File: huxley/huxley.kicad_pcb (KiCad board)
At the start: 4 copper layers, 150 x 150 mm, 101 parts, among them J1 CT3151V1-2, J11 SMA_RF2-04A-T-00-50-G, J13 SMA_RF2-04A-T-00-50-G, J15 SMA_RF2-04A-T-00-50-G, J17 SMA_RF2-04A-T-00-50-G, J18 SMA_RF2-04A-T-00-50-G, J19 SMA_RF2-04A-T-00-50-G, J2 CT3151V1-2, J20 SMA_RF2-04A-T-00-50-G, J21 61300211121, J22 SMA_RF2-04A-T-00-50-G, J24 CT3151V1-2, J25 61300211121, J26 61300211121, J27 61300211121, J28 61300211121, J29 61300211121, J3 CT3151V1-2, J30 61300211121, J31 61300211121, J32 61300211121, J33 67996-130HLF, J34 CT3151V1-0, J35 CT3151V1-2, J37 CT3151V1-0, J39 CT3151V1-2, J4 SMA_RF2-04A-T-00-50-G, J5 SMA_RF2-04A-T-00-50-G, J7 SMA_RF2-04A-T-00-50-G, J9 SMA_RF2-04A-T-00-50-G, U2 LM134H, U3 MAX40201FAUA+, U4 TMUX1112PWR, U5 TMUX1112PWR, U6 NVT2010PW_118

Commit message: layout_1003_2
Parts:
- U1: footprint _726_Common:CPG08462 -> 0_726_footprints:CPG08462_Full
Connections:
- U1 pad A1: PP_VDDIO_1V8 -> unconnected-(U1D-VDDPST-PadA1)
- U1 pad A11: GND -> unconnected-(U1F-VSS-PadA11)
- U1 pad A4: GND -> unconnected-(U1F-VSS-PadA4)
- U1 pad A5: PP_VDD_0V9 -> unconnected-(U1D-VDD-PadA5)
- U1 pad A7: PP_VDDIO_1V8 -> unconnected-(U1D-VDDPST_POC-PadA7)
- U1 pad D1: PP_VDD_0V9 -> unconnected-(U1D-VDD-PadD1)
- U1 pad D11: PP_VDD_0V9 -> unconnected-(U1D-VDD-PadD11)
- U1 pad E11: PP_TAVDD_1V8 -> unconnected-(U1E-TAVDD-PadE11)
- U1 pad G1: PP_TAVDD_1V8 -> unconnected-(U1E-TAVDD-PadG1)
- U1 pad K1: GND -> unconnected-(U1F-VSS-PadK1)
- U1 pad L1: GND -> unconnected-(U1F-VSS-PadL1)
- U1 pad L11: GND -> unconnected-(U1F-VSS-PadL11)
- U1 pad L7: GND -> unconnected-(U1F-VSS-PadL7)
- U1 pad L8: PP_TAVDD_1V8 -> unconnected-(U1E-TAVDD-PadL8)

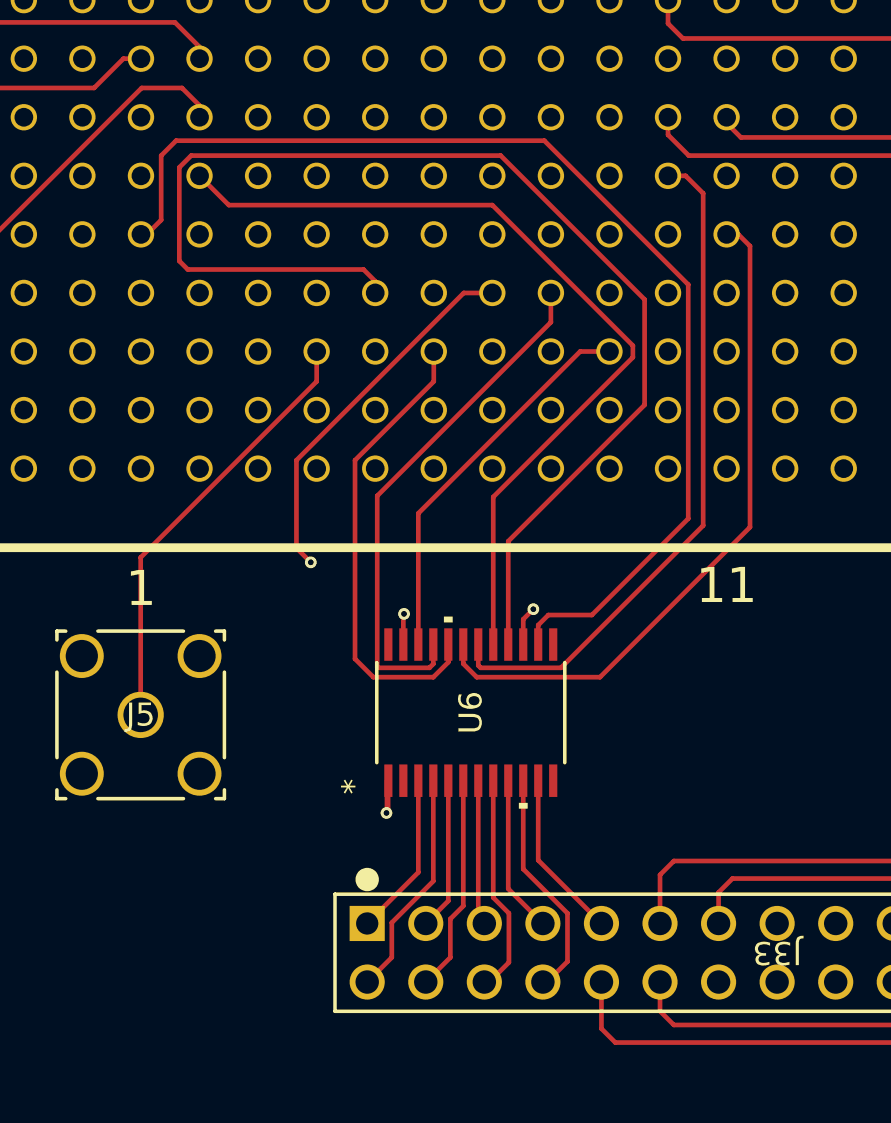
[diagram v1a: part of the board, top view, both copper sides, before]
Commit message: reorganized pin assignment to level shifter; matched 3V3 power net name; minor schematic cleanup
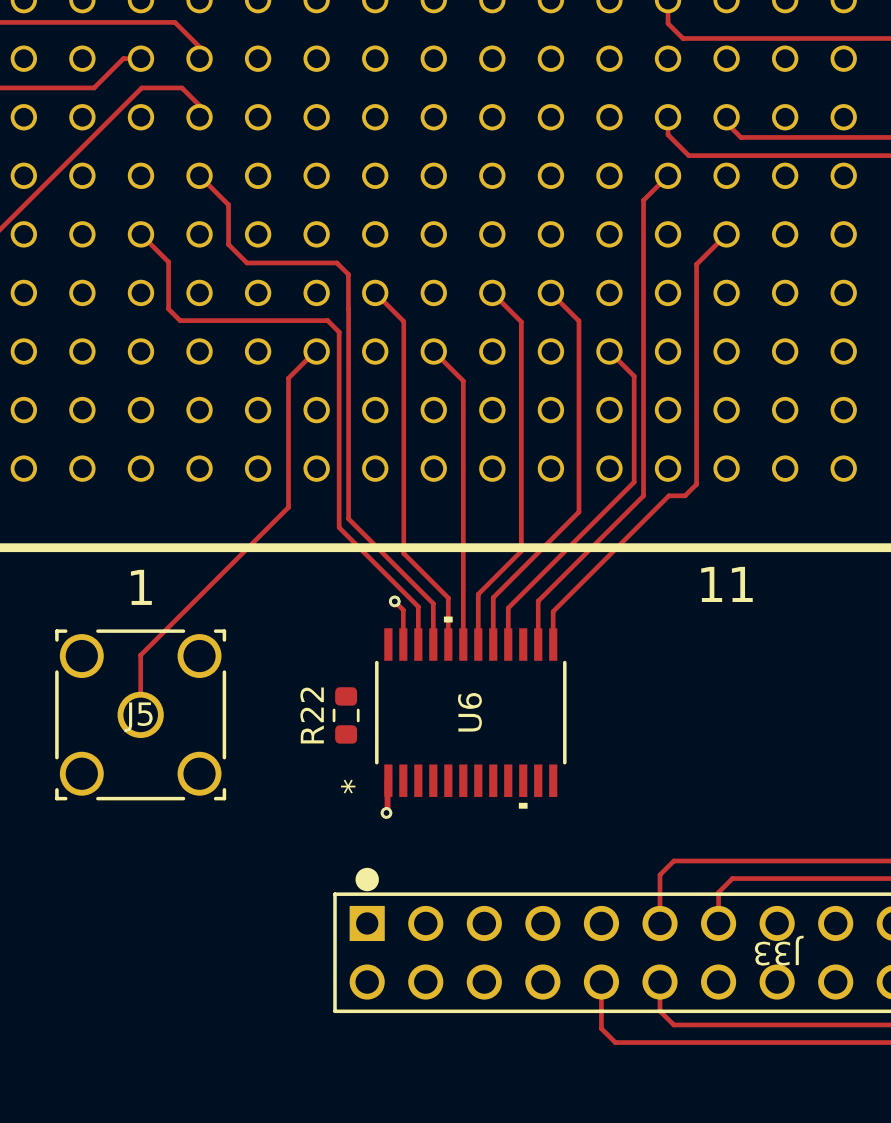
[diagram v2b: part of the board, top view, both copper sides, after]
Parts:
- added R22: 10k, Resistor_SMD:R_0603_1608Metric, F.Cu at (101.1, 145.3)
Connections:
- C13 pad 1: +3.3V -> PP_SYS_3V3
- C14 pad 1: +3.3V -> PP_SYS_3V3
- C15 pad 1: +3.3V -> PP_SYS_3V3
- C16 pad 1: +3.3V -> PP_SYS_3V3
- C17 pad 1: +3.3V -> PP_SYS_3V3
- C18 pad 1: +3.3V -> PP_SYS_3V3
- C19 pad 1: +3.3V -> PP_SYS_3V3
- C28 pad 1: +3.3V -> PP_SYS_3V3
- C29 pad 1: +3.3V -> PP_SYS_3V3
- C30 pad 1: +3.3V -> PP_SYS_3V3
- C31 pad 1: +3.3V -> PP_SYS_3V3
- J33 pad 14: unconnected-(J33-Pad14) -> LVLS_EN
- J35 pad 1: +3.3V -> PP_SYS_3V3
- J35 pad 2: +3.3V -> PP_SYS_3V3
- J35 pad 3: +3.3V -> PP_SYS_3V3
- J35 pad 4: +3.3V -> PP_SYS_3V3
- U1 pad A1: unconnected-(U1D-VDDPST-PadA1) -> PP_VDDIO_1V8
- U1 pad A11: unconnected-(U1F-VSS-PadA11) -> GND
- U1 pad A4: unconnected-(U1F-VSS-PadA4) -> GND
- U1 pad A5: unconnected-(U1D-VDD-PadA5) -> PP_VDD_0V9
- U1 pad A7: unconnected-(U1D-VDDPST_POC-PadA7) -> PP_VDDIO_1V8
- U1 pad D1: unconnected-(U1D-VDD-PadD1) -> PP_VDD_0V9
- U1 pad D11: unconnected-(U1D-VDD-PadD11) -> PP_VDD_0V9
- U1 pad E11: unconnected-(U1E-TAVDD-PadE11) -> PP_TAVDD_1V8
- U1 pad G1: unconnected-(U1E-TAVDD-PadG1) -> PP_TAVDD_1V8
- U1 pad K1: unconnected-(U1F-VSS-PadK1) -> GND
- U1 pad L1: unconnected-(U1F-VSS-PadL1) -> GND
- U1 pad L11: unconnected-(U1F-VSS-PadL11) -> GND
- U1 pad L7: unconnected-(U1F-VSS-PadL7) -> GND
- U1 pad L8: unconnected-(U1E-TAVDD-PadL8) -> PP_TAVDD_1V8
- U3 pad 8: +3.3V -> PP_SYS_3V3
- U4 pad 13: +3.3V -> PP_SYS_3V3
- U5 pad 13: +3.3V -> PP_SYS_3V3
- U6 pad 10: SPI_CIPO_3V3 -> unconnected-(U6-A8-Pad10)
- U6 pad 11: TSCAN_OUT_3V3 -> SCAN_EN_3V3
- U6 pad 12: unconnected-(U6-A10-Pad12) -> RST_L_3V3
- U6 pad 13: unconnected-(U6-B10-Pad13) -> RST_L
- U6 pad 14: TSCAN_OUT -> SCAN_EN
- U6 pad 15: SPI_CIPO -> unconnected-(U6-B8-Pad15)
- U6 pad 16: IO_UCLK -> SPI_CS_L
- U6 pad 17: TSCAN_EN -> SPI_CLK
- U6 pad 18: SCAN_EN -> SPI_CIPO
- U6 pad 19: RST_L -> SPI_COPI
- U6 pad 20: SPI_COPI -> IO_UCLK
- U6 pad 21: SPI_CLK -> TSCAN_EN
- U6 pad 22: SPI_CS_L -> TSCAN_OUT
- U6 pad 23: PP_VDD_0V9 -> PP_VDDIO_1V8
- U6 pad 3: SPI_CS_L_3V3 -> TSCAN_OUT_3V3
- U6 pad 4: SPI_CLK_3V3 -> TSCAN_EN_3V3
- U6 pad 5: SPI_COPI_3V3 -> IO_UCLK_3V3
- U6 pad 6: RST_L_3V3 -> SPI_COPI_3V3
- U6 pad 7: SCAN_EN_3V3 -> SPI_CIPO_3V3
- U6 pad 8: TSCAN_EN_3V3 -> SPI_CLK_3V3
- U6 pad 9: IO_UCLK_3V3 -> SPI_CS_L_3V3
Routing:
- net IO_UCLK: track 53.8 -> 16.6 mm
- net TSCAN_OUT: track 49.1 -> 26.5 mm
- net PP_SYS_3V3: track 0.00 -> 20.2 mm, vias 0 -> 12
- net +3.3V: track 20.2 -> 0.00 mm, vias 12 -> 0
- net SPI_CIPO: track 29.1 -> 16.5 mm, vias 2 -> 0
- net TSCAN_EN: track 37.3 -> 26.8 mm
- net SPI_CIPO_3V3: track 10.1 -> 0.00 mm
- net SPI_CLK_3V3: track 9.92 -> 0.00 mm
- net TSCAN_EN_3V3: track 9.58 -> 0.00 mm
- net RST_L_3V3: track 9.41 -> 0.00 mm
- net RST_L: track 29.6 -> 21.3 mm
- net TSCAN_OUT_3V3: track 7.33 -> 0.00 mm
- net SPI_CS_L_3V3: track 7.11 -> 0.00 mm
- net SPI_COPI: track 20.2 -> 13.2 mm
- net SCAN_EN: track 29.5 -> 22.7 mm
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- added copper zone on In2.Cu, net PP_SYS_3V3
- removed copper zone on In2.Cu, net +3.3V

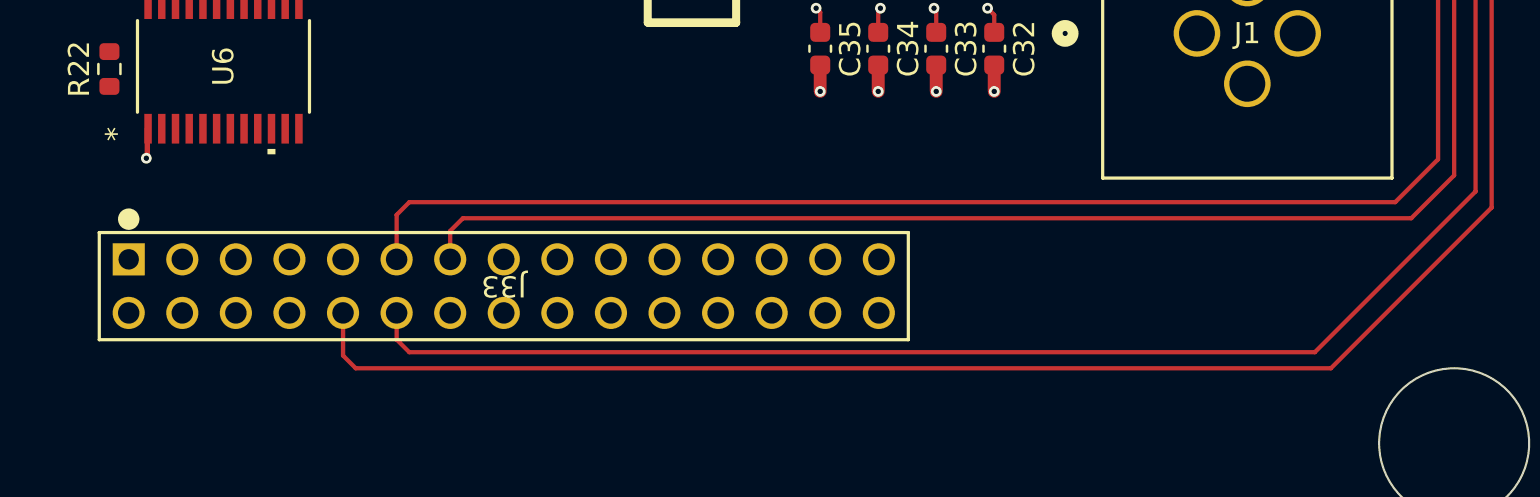
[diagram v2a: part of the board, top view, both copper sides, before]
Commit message: quick remap of 30pin
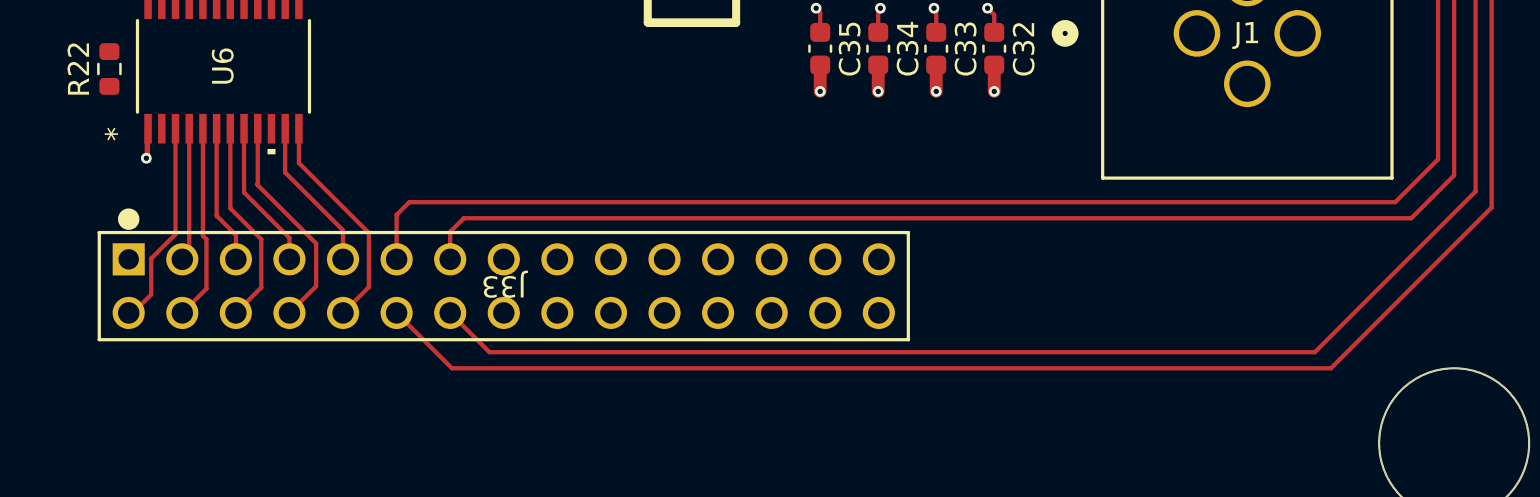
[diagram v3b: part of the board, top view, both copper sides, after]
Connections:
- J33 pad 1: SPI_CS_L_3V3 -> LVLS_EN
- J33 pad 10: IBIAS_SEL1 -> RST_L_3V3
- J33 pad 12: IBIAS_SEL3 -> IBIAS_SEL1
- J33 pad 14: LVLS_EN -> IBIAS_SEL3
- J33 pad 2: SPI_CLK_3V3 -> TSCAN_OUT_3V3
- J33 pad 3: SPI_COPI_3V3 -> TSCAN_EN_3V3
- J33 pad 4: RST_L_3V3 -> IO_UCLK_3V3
- J33 pad 5: SCAN_EN_3V3 -> SPI_COPI_3V3
- J33 pad 6: TSCAN_EN_3V3 -> SPI_CIPO_3V3
- J33 pad 7: IO_UCLK_3V3 -> SPI_CLK_3V3
- J33 pad 8: SPI_CIPO_3V3 -> SPI_CS_L_3V3
- J33 pad 9: TSCAN_OUT_3V3 -> SCAN_EN_3V3
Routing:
- net RST_L_3V3: track 0.00 -> 10.6 mm
- net SPI_CS_L_3V3: track 0.00 -> 10.4 mm
- net SPI_CIPO_3V3: track 0.00 -> 9.84 mm
- net TSCAN_OUT_3V3: track 0.00 -> 9.77 mm
- net IO_UCLK_3V3: track 0.00 -> 9.28 mm
- net SCAN_EN_3V3: track 0.00 -> 7.33 mm
- net SPI_CLK_3V3: track 0.00 -> 7.08 mm
- net SPI_COPI_3V3: track 0.00 -> 6.57 mm
- net TSCAN_EN_3V3: track 0.00 -> 6.33 mm
- net IBIAS_SEL1: track 239.9 -> 236.1 mm
- net IBIAS_SEL3: track 230.0 -> 226.8 mm

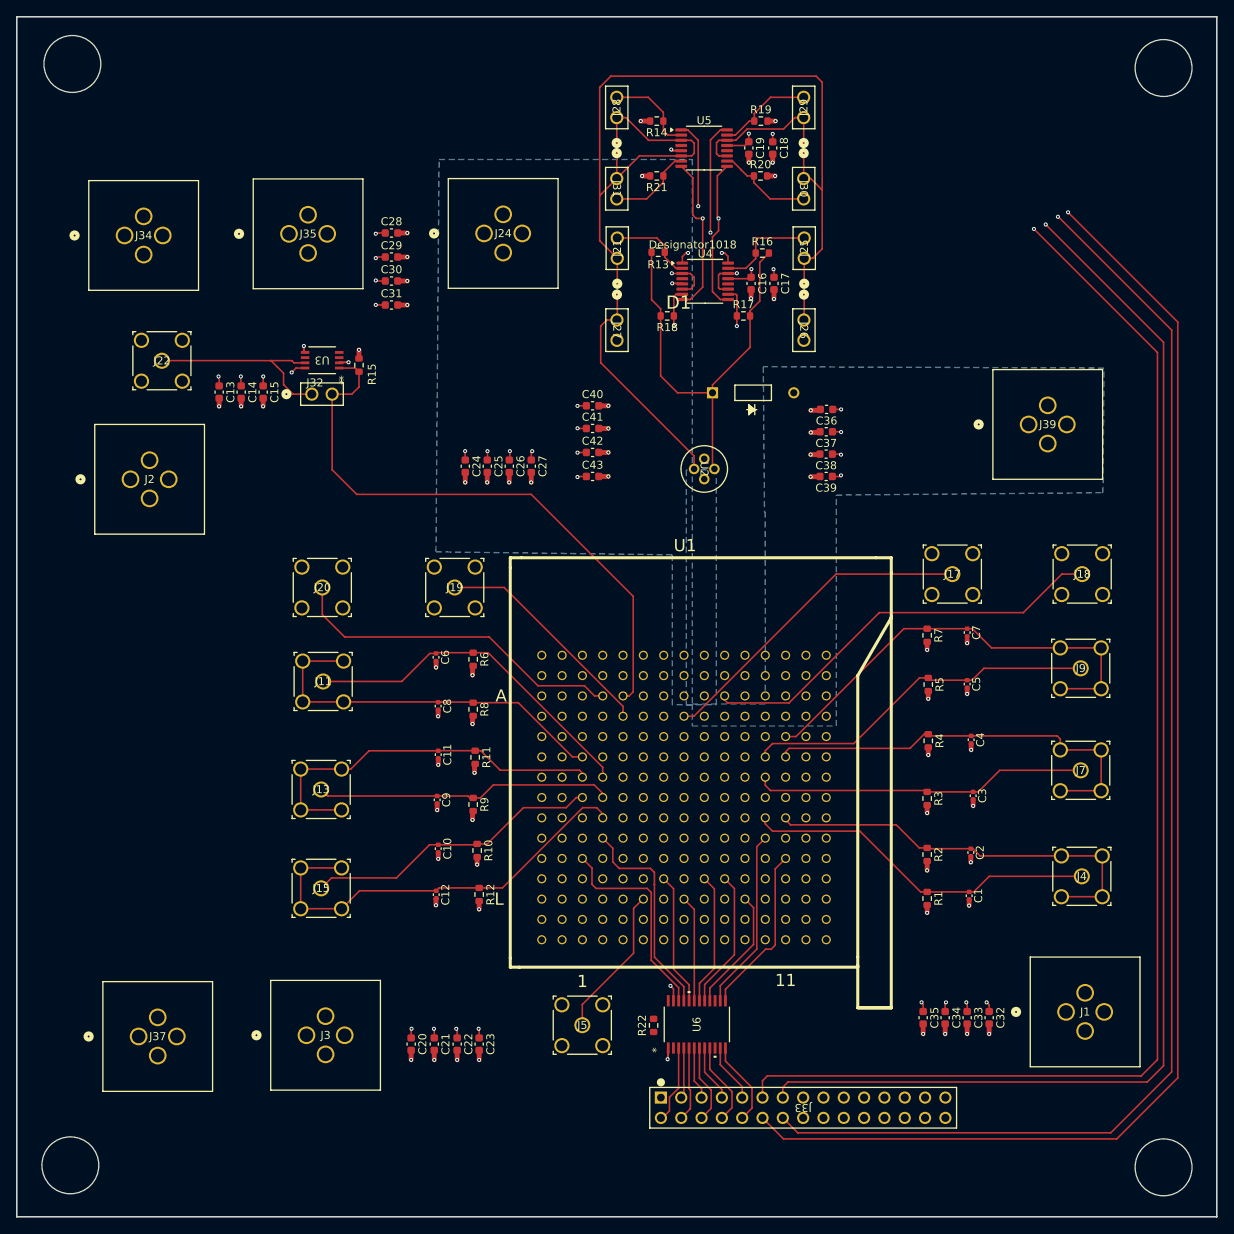
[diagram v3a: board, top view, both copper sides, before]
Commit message: fixed all bad refs; replaced analog discovery connector; change level shifter 3v3 to from analog discovery
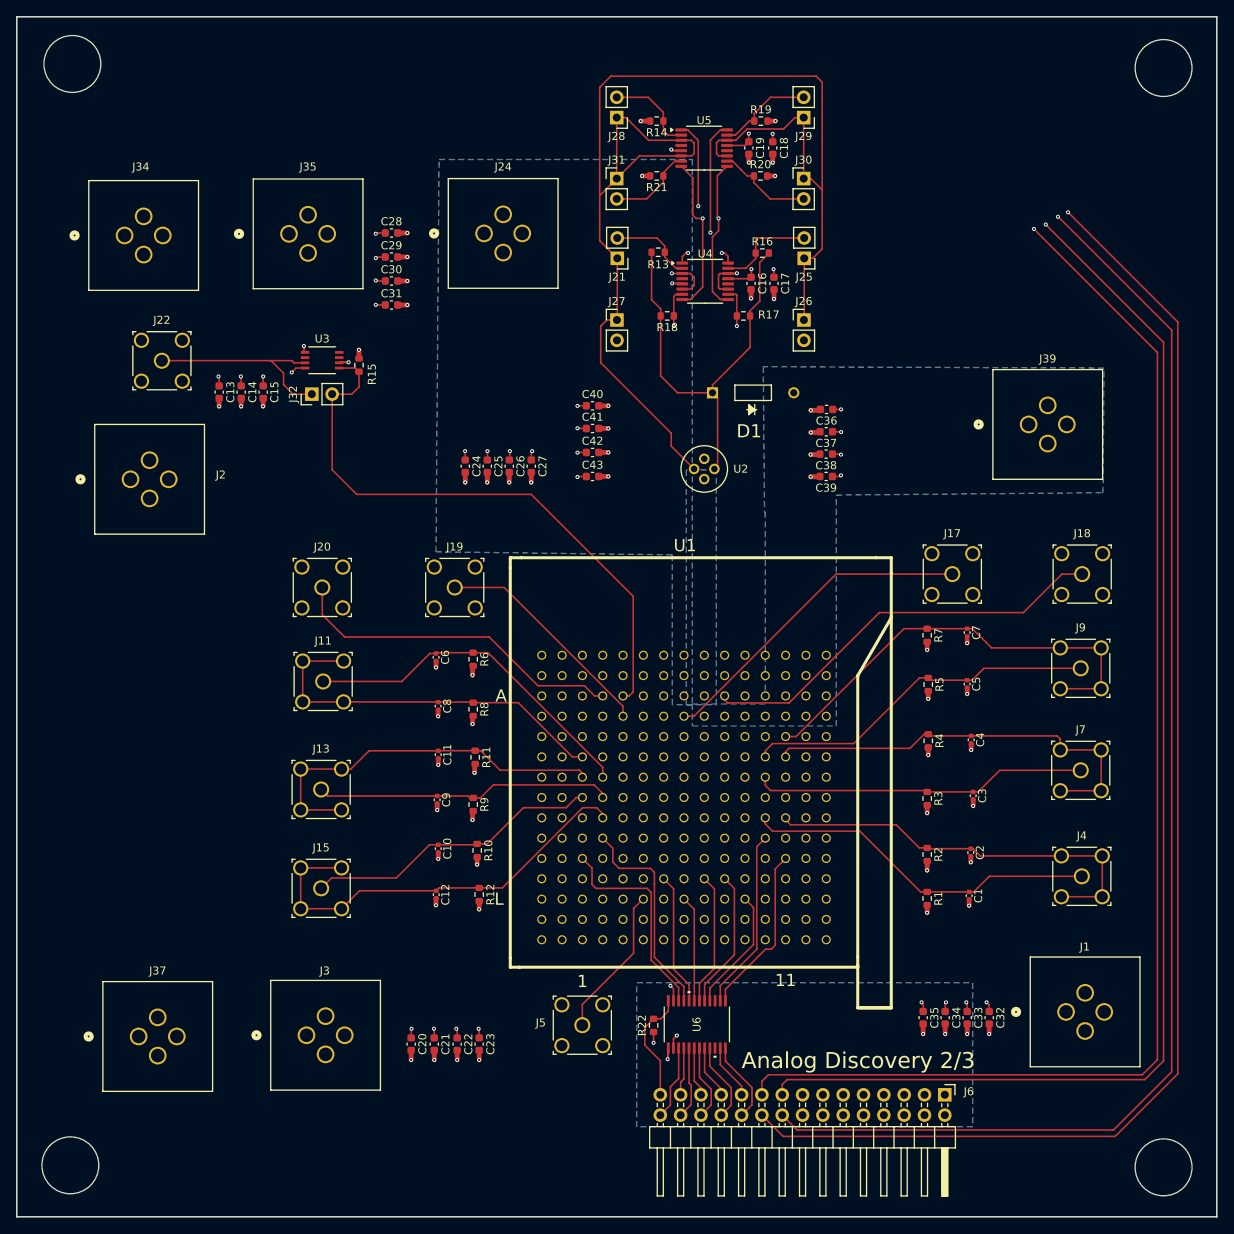
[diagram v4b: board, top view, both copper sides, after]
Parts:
- removed J33: 67996-130HLF, 726_footprints:30p_connector
- added J6: ~, Connector_PinHeader_2.54mm:PinHeader_2x15_P2.54mm_Horizontal, F.Cu at (137.5, 154.0)
- D1: footprint 726_footprints:DIO_1N457 -> 0_726_footprints:DIO_1N457
- J1, J2, J24, J3, J34, J35, J37, J39: footprint 726_footprints:banana_plug_CT3151V1-0 -> 0_726_footprints:banana_plug_CT3151V1-0
- J11, J13, J15, J17, J18, J19, J20, J22, J4, J5, J7, J9: footprint 726_footprints:CONN_RF2-04A-T-00-50-G_ADM -> 0_726_footprints:CONN_RF2-04A-T-00-50-G_ADM
- J21, J25, J26, J27, J28, J29, J30, J31, J32: footprint 726_footprints:CONN_61300211121_WRE -> Connector_PinHeader_2.54mm:PinHeader_1x02_P2.54mm_Vertical
- U2: footprint 726_footprints:lm134 -> 0_726_footprints:lm134
- U3: footprint 726_footprints:MAX40201FAUA+ -> 0_726_footprints:MAX40201FAUA+
- U6: footprint _726_Common:TSSOP24_SOT355-1_NXP -> 0_726_footprints:TSSOP24_SOT355-1_NXP
- turned J21 to 180 degrees
- turned J25 to 180 degrees
- turned J26 to 0 degrees
- turned J27 to 0 degrees
- turned J28 to 180 degrees
- turned J29 to 180 degrees
- turned J30 to 0 degrees
- turned J31 to 0 degrees
- turned J32 to 90 degrees
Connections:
- R22 pad 1: PP_SYS_3V3 -> PP_AD2_3V3
- U6 pad 2: PP_SYS_3V3 -> PP_AD2_3V3
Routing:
- net LVLS_EN: track 0.00 -> 14.3 mm
- net PP_AD2_3V3: track 0.00 -> 3.08 mm, vias 0 -> 2
- added copper zone on B.Cu, net PP_AD2_3V3
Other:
- board text added: "Analog Discovery 2/3"
- board text removed: "Designator1018"
